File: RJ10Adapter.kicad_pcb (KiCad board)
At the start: 2 copper layers, 73.1 x 18.3 mm, 14 parts, among them J1 RJ10, J2 Conn_01x06_Male, J3 USB_B_Micro, SW1 SW_Push, U1 AMS1117-3.3, U2 ESP-12F

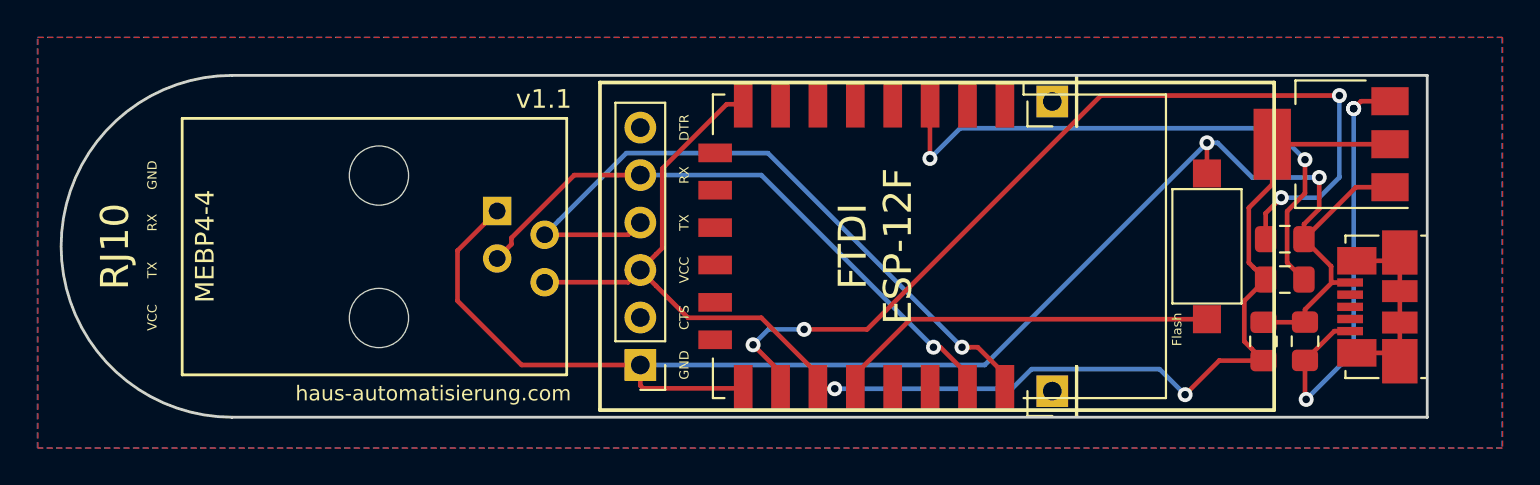
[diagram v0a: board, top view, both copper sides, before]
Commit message: Resistor to GPIO
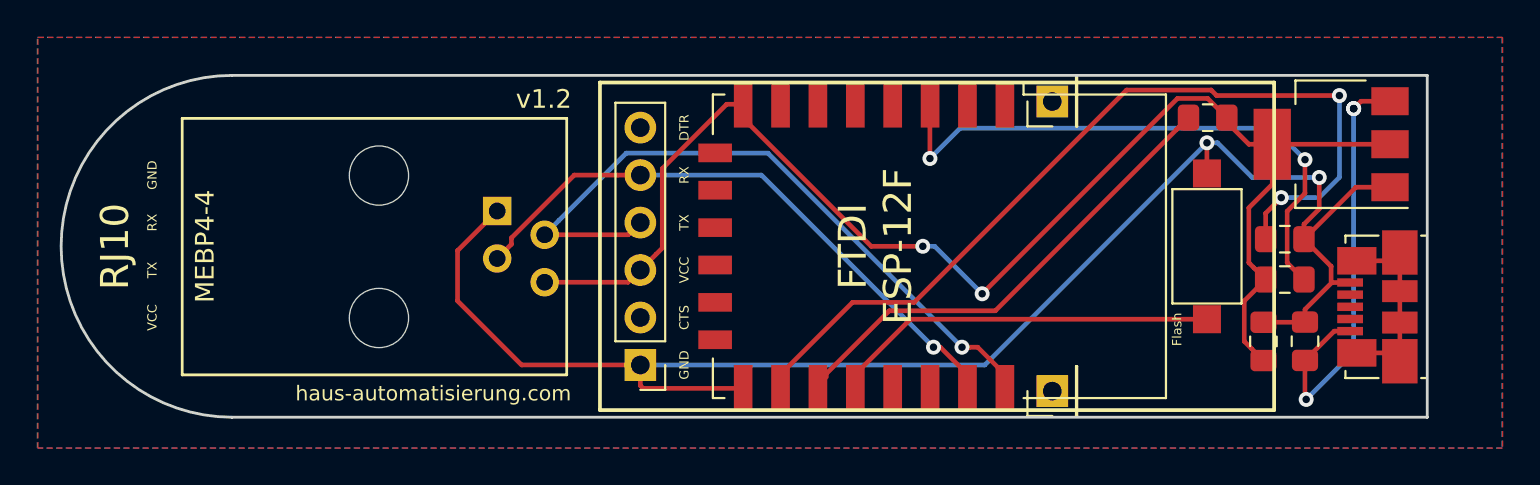
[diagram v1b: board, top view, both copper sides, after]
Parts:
- added R3: R, Resistor_SMD:R_0805_2012Metric_Pad1.15x1.40mm_HandSolder, F.Cu at (174.6, 89.6)
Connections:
- U2 pad 17: /Vin -> Net-(R3-Pad2)
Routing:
- net Net-(R3-Pad2): track 0.00 -> 26.9 mm
- net Net-(R2-Pad2): track 50.3 -> 48.4 mm, vias 4 -> 2
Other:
- board text added: "v1.2"
- board text removed: "v1.1"

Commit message: added resistor
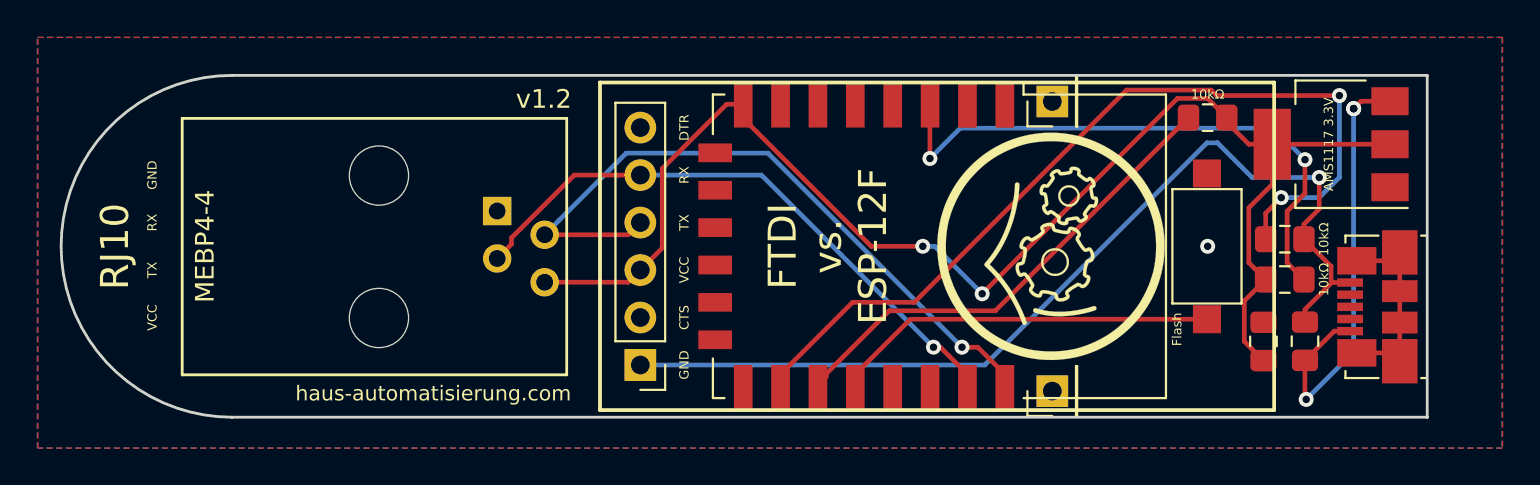
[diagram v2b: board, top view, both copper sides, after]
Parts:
- added G***: LOGO, libs:Logo, F.Cu at (166.2, 96.5)
- C1, C2: value C -> 100µF
- J1: footprint libs:MEBP_44S_MK -> halibs:MEBP_44S
- R1, R2, R3: value R -> 10kΩ
- turned G*** to 270 degrees
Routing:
- net GND: track 85.5 -> 52.3 mm
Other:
- board text added: "10kΩ"
- board text added: "AMS1117 3.3V"
- board text added: "FTDI vs. ESP-12F"
- board text removed: "FTDI ESP-12F"
